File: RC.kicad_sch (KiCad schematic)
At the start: 41 parts, among them J13 Conn_01x01_Pin, J14 Conn_01x01_Pin, J15 Conn_01x01_Pin, Q25 NMOS, Q26 NMOS, Q27 NMOS, Q28 NMOS, Q29 NMOS, Q30 NMOS, U10 MCT8329A1IREER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

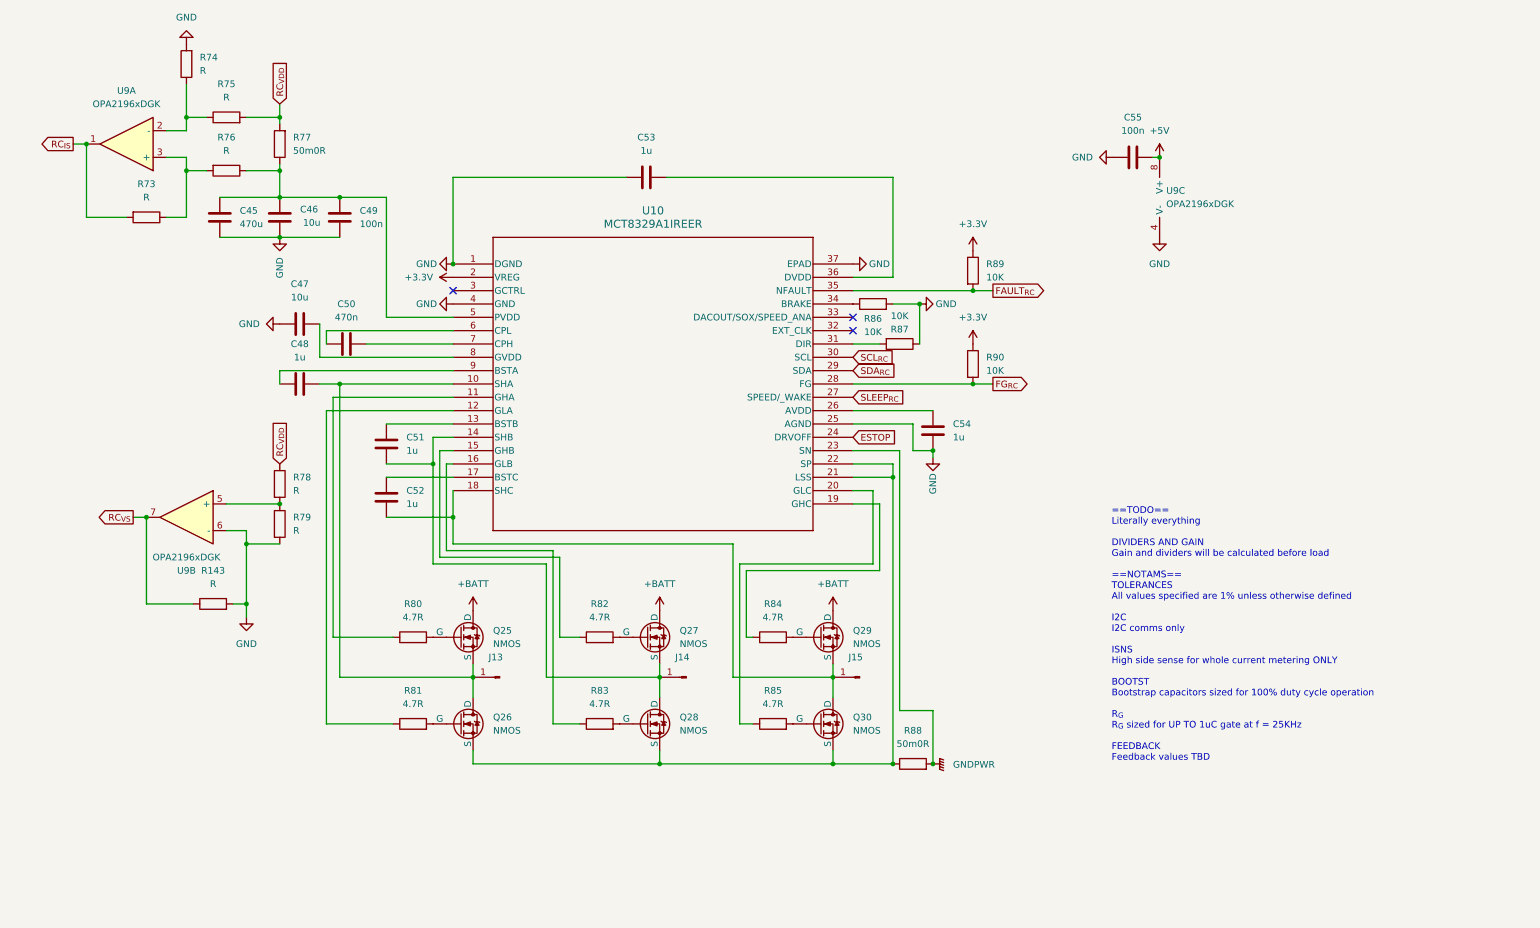
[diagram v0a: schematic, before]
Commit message: The great decluttering
Moved all possible controls to I2C, part selection commenced, IOs assigned pending comms schema
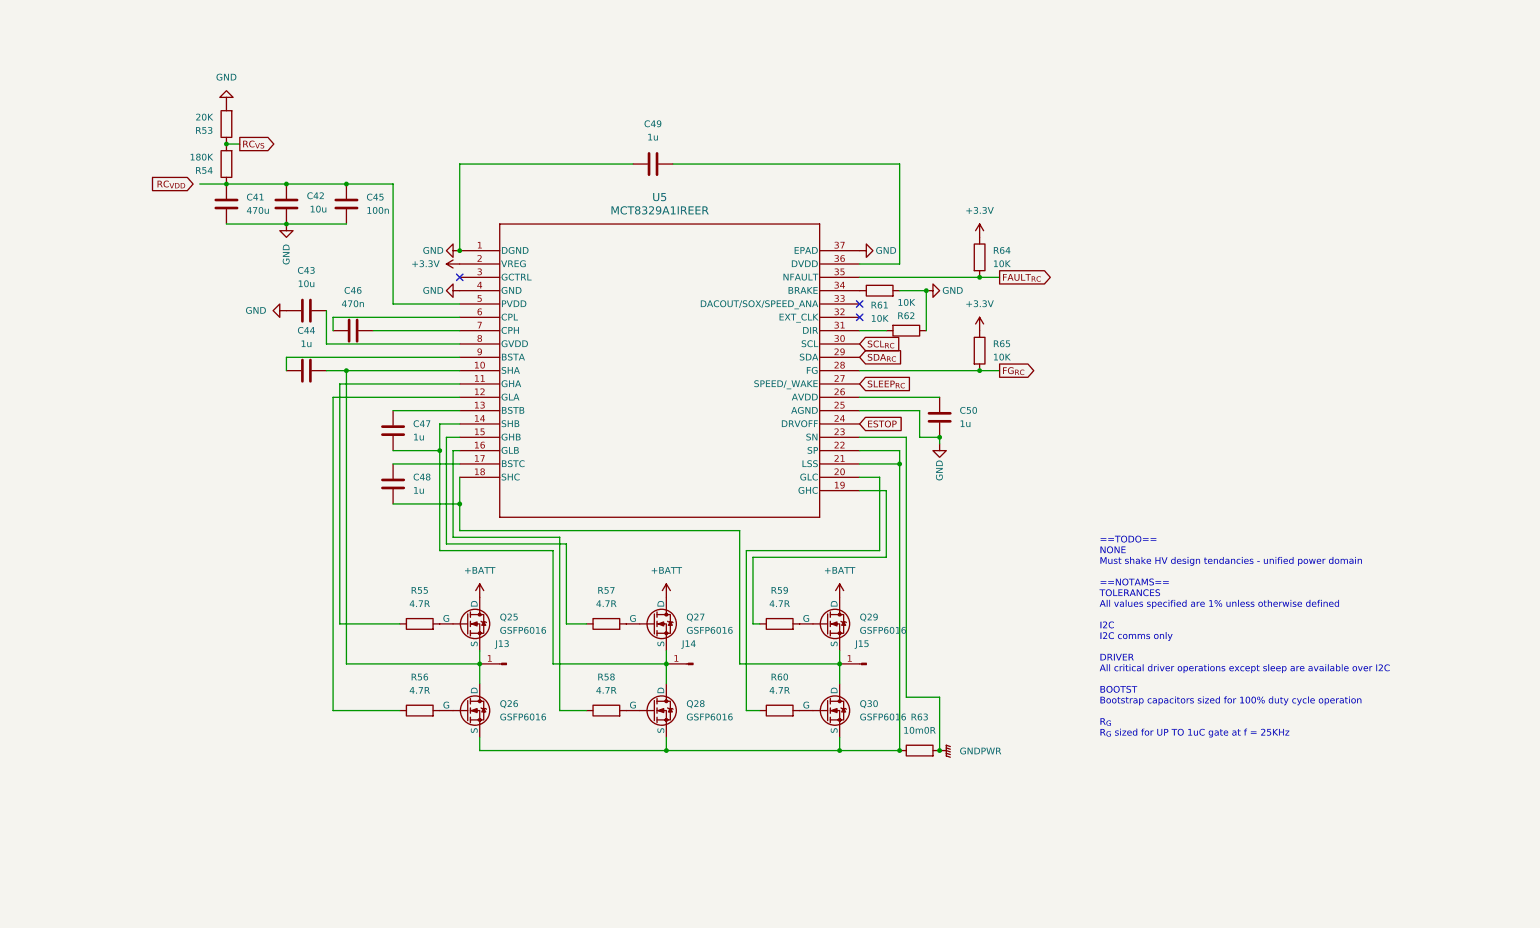
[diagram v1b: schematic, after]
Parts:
- removed C51, C52, C53, C54: 1u, Capacitor_SMD:C_0603_1608Metric, symbol Device:C
- removed C55: 100n, Capacitor_SMD:C_0603_1608Metric, symbol Device:C
- removed R143, R73, R74, R75, R76, R78, R79: R, Resistor_SMD:R_0603_1608Metric_Pad0.98x0.95mm_HandSolder, symbol Device:R
- removed R77, R88: 50m0R, Resistor_SMD:R_1206_3216Metric, symbol Device:R
- removed R80, R81, R82, R83, R84, R85: 4.7R, Resistor_SMD:R_1206_3216Metric, symbol Device:R
- removed R86, R87, R89, R90: 10K, Resistor_SMD:R_0603_1608Metric_Pad0.98x0.95mm_HandSolder, symbol Device:R
- removed U10: MCT8329A1IREER, footprints:WQFN36_REE_TEX, symbol MCT8329:MCT8329A1IREER
- removed U9: OPA2196xDGK, Package_SO:VSSOP-8_3x3mm_P0.65mm, symbol Amplifier_Operational:OPA2196xDGK
- added C41: 470u, Capacitor_SMD:C_0603_1608Metric, symbol Device:C
- added C42, C43: 10u, Capacitor_SMD:C_0603_1608Metric, symbol Device:C
- added C44: 1u, Capacitor_SMD:C_0603_1608Metric, symbol Device:C
- added R53: 20K, Resistor_SMD:R_0603_1608Metric_Pad0.98x0.95mm_HandSolder, symbol Device:R
- added R54: 180K, Resistor_SMD:R_0603_1608Metric_Pad0.98x0.95mm_HandSolder, symbol Device:R
- added R55, R56, R57, R58, R59, R60: 4.7R, Resistor_SMD:R_1206_3216Metric, symbol Device:R
- added R61, R62, R64, R65: 10K, Resistor_SMD:R_0603_1608Metric_Pad0.98x0.95mm_HandSolder, symbol Device:R
- added R63: 10m0R, Resistor_SMD:R_1206_3216Metric, symbol Device:R
- added U5: MCT8329A1IREER, footprints:WQFN36_REE_TEX, symbol MCT8329:MCT8329A1IREER
- C45: value 470u -> 100n
- C46: value 10u -> 470n
- C47: value 10u -> 1u
- C49: value 100n -> 1u
- C50: value 470n -> 1u
- Q25, Q26, Q27, Q28, Q29, Q30: value NMOS -> GSFP6016; footprint (none) -> Package_DFN_QFN:PQFN-8-EP_6x5mm_P1.27mm_Generic
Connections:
- net +3.3V: now also R64.1, R65.1, U5.2 (VREG)
- net ESTOP: now also U5.24 (DRVOFF)
- net FAULT_{RC}: now also R64.2, U5.35 (NFAULT)
- net FG_{RC}: now also R65.2, U5.28 (FG)
- net GND: now also C49.1, C50.1, C41.2, C42.2, C43.1, R53.2, R61.2, R62.1, U5.1 (DGND), U5.25 (AGND), U5.37 (EPAD), U5.4 (GND); no longer C46.2, C47.1, C49.2
- net GNDPWR: now also R63.2, U5.23 (SN)
- net RC_{VS}: now also R53.1, R54.2
- net SCL_{RC}: now also U5.30 (SCL)
- net SDA_{RC}: now also U5.29 (SDA)
- net SLEEP_{RC}: now also U5.27 (SPEED/_WAKE)
- net at C47.2: now also J14.1 (Pin_1), Q27.3 (S), Q28.1 (D), U5.14 (SHB)
- net at Q28.2 (G): now also R58.2
- net at Q26.3 (S), Q28.3 (S), Q30.3 (S): now also R63.1, U5.21 (LSS), U5.22 (SP)
- net at J15.1 (Pin_1), Q29.3 (S), Q30.1 (D): now also C48.2, U5.18 (SHC)
- net at Q27.2 (G): now also R57.2
- net at Q29.2 (G): now also R59.2
- net at Q25.2 (G): now also R55.2
- net at J13.1 (Pin_1), Q25.3 (S), Q26.1 (D): now also C44.1, U5.10 (SHA); no longer C48.1
- net at Q26.2 (G): now also R56.2
- net at Q30.2 (G): now also R60.2
- net at C50.2: now also U5.26 (AVDD)
- new net: R59.1, U5.19 (GHC)
- new net: C41.1, C42.1, C45.1, R54.1, U5.5 (PVDD)
- new net: C43.2, U5.8 (GVDD)
- new net: C48.1, U5.17 (BSTC)
- new net: R61.1, U5.34 (BRAKE)
- new net: R60.1, U5.20 (GLC)
- new net: R62.2, U5.31 (DIR)
- new net: C46.1, U5.6 (CPL)
- new net: C46.2, U5.7 (CPH)
- new net: R56.1, U5.12 (GLA)
- new net: R55.1, U5.11 (GHA)
- new net: C47.1, U5.13 (BSTB)
- new net: R58.1, U5.16 (GLB)
- new net: C44.2, U5.9 (BSTA)
- new net: R57.1, U5.15 (GHB)
- new net: C49.2, U5.36 (DVDD)
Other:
- note added: "==TODO== NONE Must shake HV design tendancies - unified power domain ==NOTAMS== TOLERANCES All values specified are 1% unless otherwise defined I2C I2C comms only DRIVER All critical driver operations except sleep are available over I2C BOOTST Bootstrap capacitors sized for 100% duty cycle operation R_{G} R_{G} sized for UP TO 1uC gate at f = 25KHz"
- note removed: "==TODO== Literally everything DIVIDERS AND GAIN Gain and dividers will be calculated before load ==NOTAMS== TOLERANCES All values specified are 1% unless otherwise defined I2C I2C comms only ISNS High side sense for whole current metering ONLY BOOTST Bootstrap capacitors sized for 100% duty cycle operation R_{G} R_{G} sized for UP TO 1uC gate at f = 25KHz FEEDBACK Feedback values TBD"

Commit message: Powerstage
Powerstage layout, non critical changes to schematic
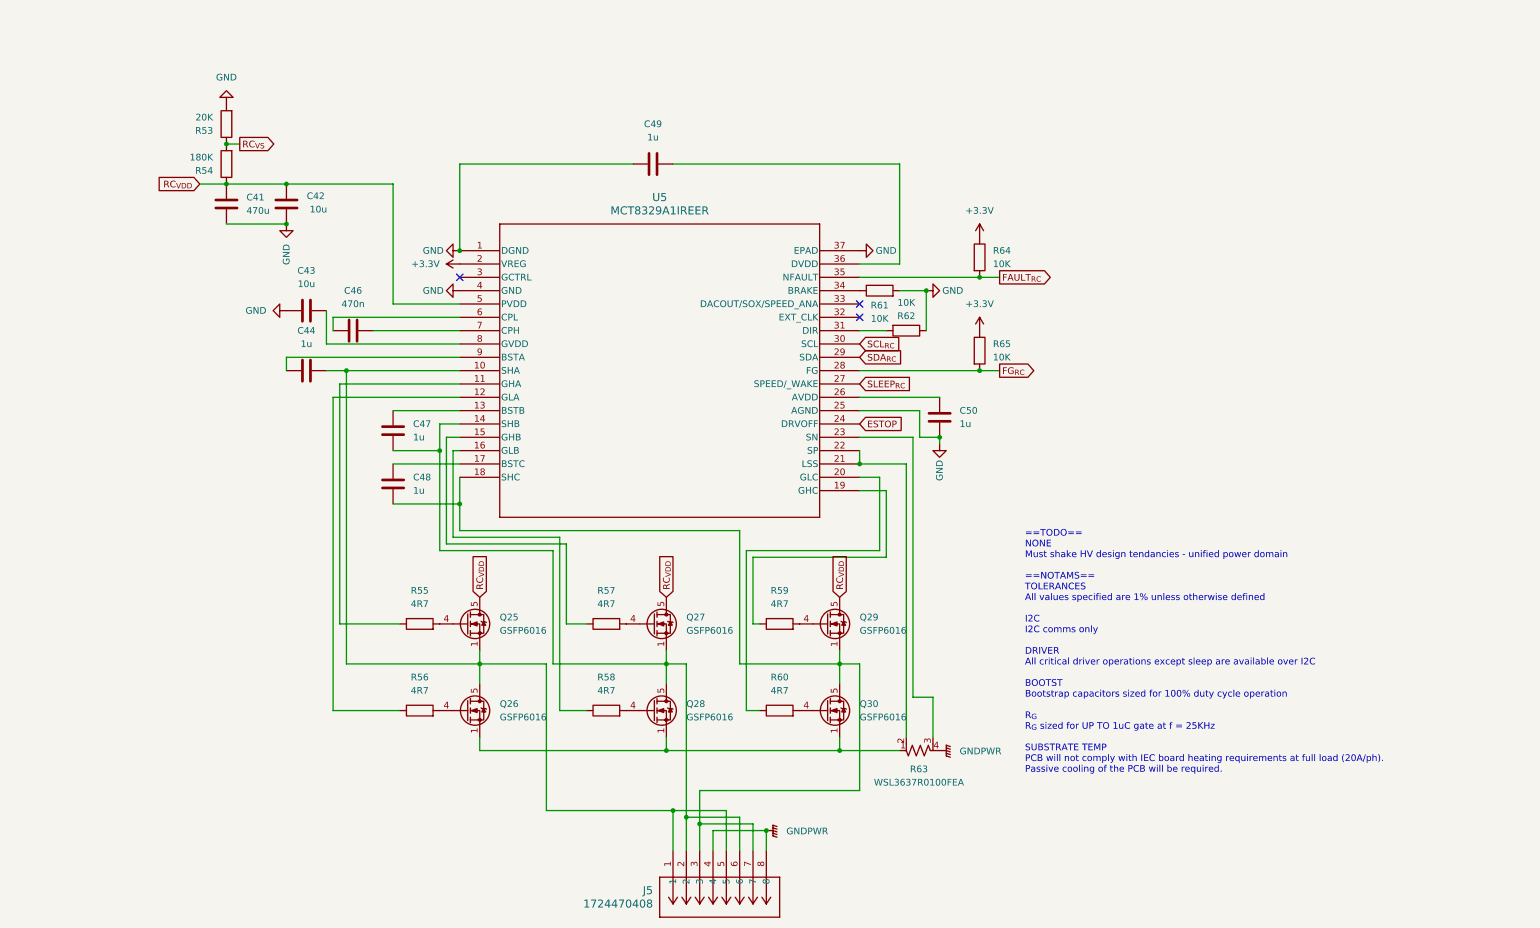
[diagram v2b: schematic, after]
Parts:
- removed C45: 100n, Capacitor_SMD:C_0603_1608Metric, symbol Device:C
- removed J13, J14, J15: Conn_01x01_Pin, symbol Connector:Conn_01x01_Pin
- removed Q25, Q26, Q27, Q28, Q29, Q30: GSFP6016, Package_DFN_QFN:PQFN-8-EP_6x5mm_P1.27mm_Generic, symbol Simulation_SPICE:NMOS
- removed R63: 10m0R, Resistor_SMD:R_1206_3216Metric, symbol Device:R
- added J5: 1724470408, footprints:CONN08_1724470408_MOL, symbol 1724470408:1724470408
- added Q25, Q26, Q27, Q28, Q29, Q30: GSFP6016, Package_SO:PowerPAK_SO-8_Single, symbol Transistor_FET:SiR696DP
- added R63: WSL3637R0100FEA, WSL3637_VIS, symbol WSL3637R0100FEA:WSL3637R0100FEA
- C41: footprint Capacitor_SMD:C_0603_1608Metric -> Capacitor_THT:CP_Radial_D10.0mm_P5.00mm
- C42: footprint Capacitor_SMD:C_0603_1608Metric -> Capacitor_SMD:C_1210_3225Metric
- C43: footprint Capacitor_SMD:C_0603_1608Metric -> Capacitor_SMD:C_0402_1005Metric
- C44, C46, C47, C48, C49, C50: footprint Capacitor_SMD:C_0603_1608Metric -> Capacitor_SMD:C_0201_0603Metric
- R53, R54, R61, R62, R64, R65: footprint Resistor_SMD:R_0603_1608Metric_Pad0.98x0.95mm_HandSolder -> Resistor_SMD:R_0201_0603Metric
- R55, R56, R57, R58, R59, R60: value 4.7R -> 4R7; footprint Resistor_SMD:R_1206_3216Metric -> Resistor_SMD:R_0603_1608Metric
- U5: footprint footprints:WQFN36_REE_TEX -> WQFN36_REE_TEX
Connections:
- net GNDPWR: now also J5.4, J5.8, R63.4; no longer U5.23 (SN)
- net RC_{VDD}: now also C41.1, C42.1, R54.1, U5.5 (PVDD), Q25.5 (D), Q27.5 (D), Q29.5 (D)
- net at C44.1, U5.10 (SHA): now also J5.1, J5.5, Q25.1 (S), Q25.2 (S), Q25.3 (S), Q26.5 (D)
- net at R59.2: now also Q29.4 (G)
- net at C47.2, U5.14 (SHB): now also J5.2, J5.6, Q27.1 (S), Q27.2 (S), Q27.3 (S), Q28.5 (D)
- net at C48.2, U5.18 (SHC): now also J5.3, J5.7, Q29.1 (S), Q29.2 (S), Q29.3 (S), Q30.5 (D)
- net at R60.2: now also Q30.4 (G)
- net at U5.21 (LSS), U5.22 (SP): now also R63.2
- net at C46.1: now also U5.7 (CPH); no longer U5.6 (CPL)
- net at C46.2: now also U5.6 (CPL); no longer U5.7 (CPH)
- net at R56.2: now also Q26.4 (G)
- net at R55.2: now also Q25.4 (G)
- net at R58.2: now also Q28.4 (G)
- net at R57.2: now also Q27.4 (G)
- new net: Q26.1 (S), Q26.2 (S), Q26.3 (S), Q28.1 (S), Q28.2 (S), Q28.3 (S), Q30.1 (S), Q30.2 (S), Q30.3 (S), R63.1
- new net: R63.3, U5.23 (SN)
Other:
- note added: "==TODO== NONE Must shake HV design tendancies - unified power domain ==NOTAMS== TOLERANCES All values specified are 1% unless otherwise defined I2C I2C comms only DRIVER All critical driver operations except sleep are available over I2C BOOTST Bootstrap capacitors sized for 100% duty cycle operation R_{G} R_{G} sized for UP TO 1uC gate at f = 25KHz SUBSTRATE TEMP PCB will not comply with IEC boar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"
- note removed: "==TODO== NONE Must shake HV design tendancies - unified power domain ==NOTAMS== TOLERANCES All values specified are 1% unless otherwise defined I2C I2C comms only DRIVER All critical driver operations except sleep are available over I2C BOOTST Bootstrap capacitors sized for 100% duty cycle operation R_{G} R_{G} sized for UP TO 1uC gate at f = 25KHz"
